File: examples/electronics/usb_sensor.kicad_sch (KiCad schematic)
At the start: 17 parts, among them J1 USB-Micro-B, J2 SWD, SW1 SPST, U1 AP2112K-3.3, U2 STM32F042, U3 SHT40

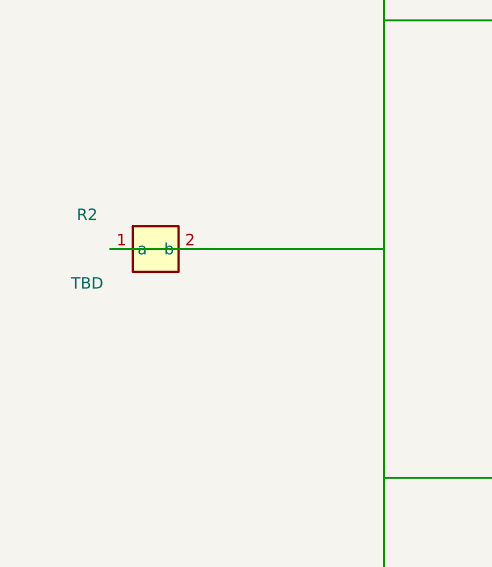
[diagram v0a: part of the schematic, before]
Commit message: feat(electronics): component laws Slice 5 — stdlib laws and fixtures
Add generic dimensioned law parameters on pin-bearing component types
(spec ForwardVoltage: Volt; spec DynamicResistance: Ohm;), including
type-level quantity defaults. Unknown spec names remain rejected outside
component bodies.

- stdlib Resistor and Wire declare always-active laws
- stdlib Diode and Led declare forward/reverse piecewise laws
- later component declarations shadow prelude declarations, so local
  same-named types cannot inherit stdlib laws by accident
- migrate led_blinker to stdlib laws and structured datasheet physics;
  the solver proves its 4.4 mA operating point
- migrate usb_sensor resistance values to structured specs; keep its
  local Resistor law-free until SPST conditional-topology state exists
- document the law mechanism and remaining fixture migration boundary

Full lib suite green; Praetor no new diagnostics; both fixtures emit.
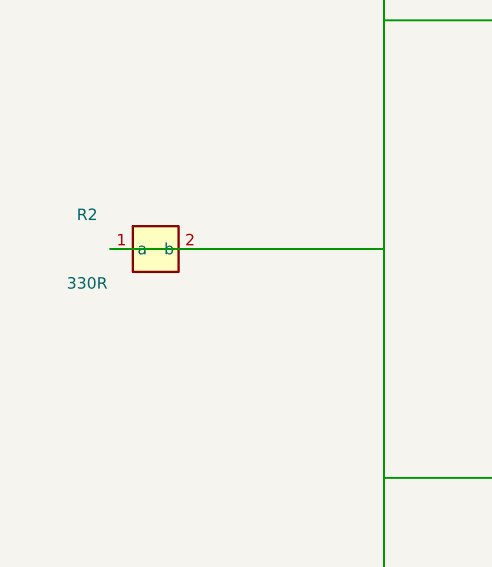
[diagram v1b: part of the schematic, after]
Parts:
- R2: value TBD -> 330R
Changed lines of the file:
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@@
     (in_bom yes) (on_board yes)
     (property "Reference" "R2" (at 93.98 300.99 0) (effects (font (size 1.27 1.27))))
-    (property "Value" "TBD" (at 93.98 308.61 0) (effects (font (size 1.27 1.27))))
+    (property "Value" "330R" (at 93.98 308.61 0) (effects (font (size 1.27 1.27))))
     (property "Footprint" "0603" (at 101.60 304.80 0) (effects (font (size 1.27 1.27)) (hide yes)))
     (instances (project briev

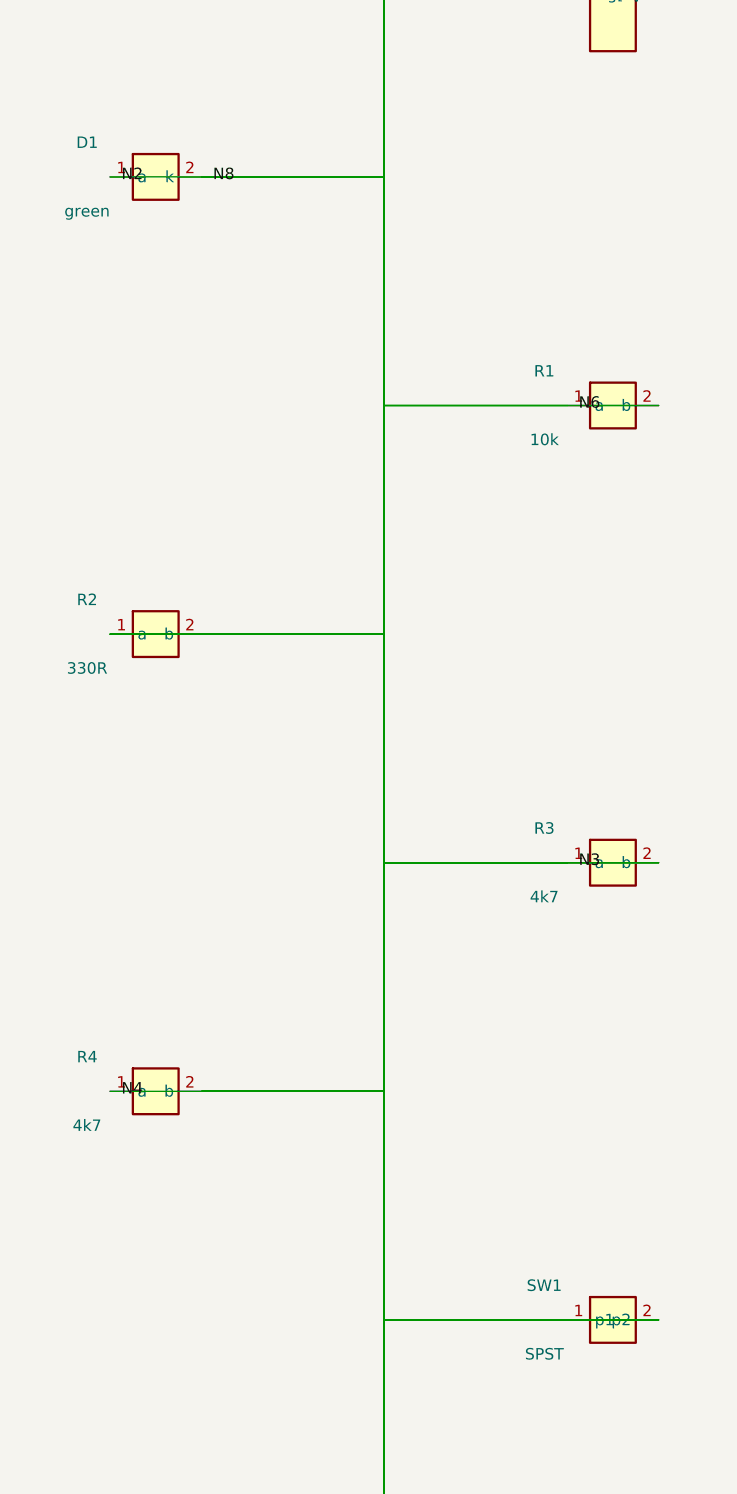
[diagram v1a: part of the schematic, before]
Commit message: feat(electronics): SPST component modes and node state selection
Add explicitly named finite component modes to the law substrate:

- parse contextual `mode <name> { … }` declarations in component bodies
- elaborate mode facts through the shared linear-law machinery
- enumerate every declared mode as a first-class DC operating state
- record instance→mode assignments and deterministic state labels
- select node-applicable states with `sw1.closed` / `!sw1.closed`
- prove node postconditions only in matching states while tolerance,
  rating, and budget checks remain all-state
- reject unknown modes and mode preconditions matching zero states
- add generic stdlib Spst with closed/open modes
- migrate usb_sensor to Spst, split pressed/released nodes, wire the
  button pull-up path, and make its local resistor law-bearing

Checked-in .ebv fixtures cover pressed/released selection and a typoed
mode selector. Full lib suite green; electronics fixtures emit; no new
Praetor diagnostics in touched analysis/parser/backend surfaces.
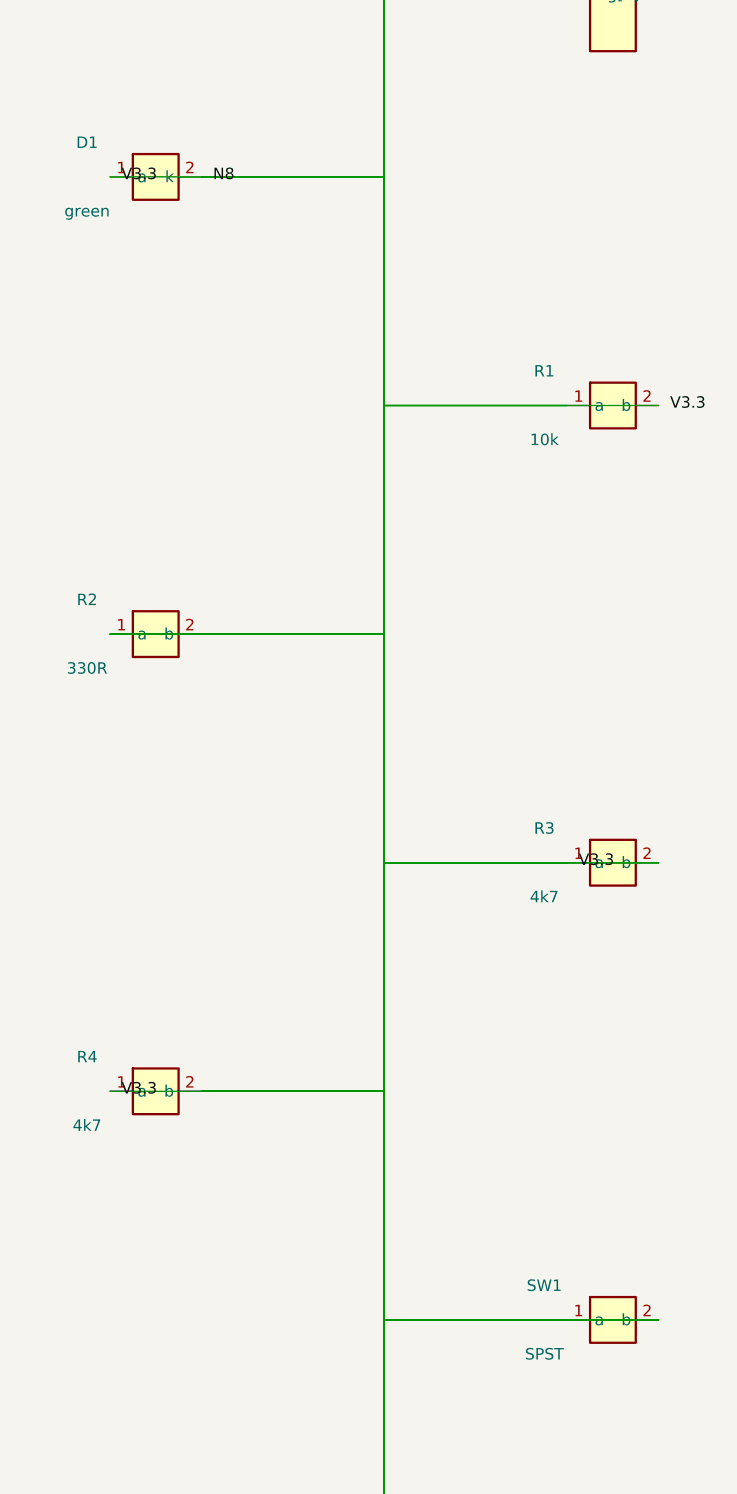
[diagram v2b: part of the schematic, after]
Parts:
- SW1: symbol Switch -> Spst
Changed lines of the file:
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@@
     ))
   )
-  (symbol (lib_id "Switch") (at 152.40 381.00 0) (unit 1)
+  (symbol (lib_id "Spst") (at 152.40 381.00 0) (unit 1)
     (in_bom yes) (on_board yes)
     (property "Reference" "SW1" (at 144.78 377.19 0) (effects (font (size 1.27 1.27))))
@@
   (wire (pts (xy 127.00 254.00) (xy 127.00 304.80)) (stroke (width 0) (type default)))
   (wire (pts (xy 127.00 304.80) (xy 106.68 304.80)) (stroke (width 0) (type default)))
-  (label "N2" (at 97.79 254.00 0) (effects (font (size 1.27 1.27)) (justify (left bottom))))
+  (label "V3.3" (at 97.79 254.00 0) (effects (font (size 1.27 1.27)) (justify (left bottom))))
   (wire (pts (xy 147.32 330.20) (xy 127.00 330.20)) (stroke (width 0) (type default)))
   (wire (pts (xy 127.00 330.20) (xy 127.00 431.80)) (stroke (width 0) (type default)))
@@
   (wire (pts (xy 127.00 431.80) (xy 127.00 455.93)) (stroke (width 0) (type default)))
   (wire (pts (xy 127.00 455.93) (xy 106.68 455.93)) (stroke (width 0) (type default)))
-  (label "N3" (at 148.59 330.20 0) (effects (font (size 1.27 1.27)) (justify (left bottom))))
+  (label "V3.3" (at 148.59 330.20 0) (effects (font (size 1.27 1.27)) (justify (left bottom))))
   (wire (pts (xy 96.52 355.60) (xy 127.00 355.60)) (stroke (width 0) (type default)))
   (wire (pts (xy 127.00 355.60) (xy 127.00 429.26)) (stroke (width 0) (type default)))
@@
   (wire (pts (xy 127.00 429.26) (xy 127.00 459.74)) (stroke (width 0) (type default)))
   (wire (pts (xy 127.00 459.74) (xy 96.52 459.74)) (stroke (width 0) (type default)))
-  (label "N4" (at 97.79 355.60 0) (effects (font (size 1.27 1.27)) (justify (left bottom))))
+  (label "V3.3" (at 97.79 355.60 0) (effects (font (size 1.27 1.27)) (justify (left bottom))))
   (wire (pts (xy 147.32 76.20) (xy 127.00 76.20)) (stroke (width 0) (type default)))
   (wire (pts (xy 127.00 76.20) (xy 127.00 101.60)) (stroke (width 0) (type default)))
@@
   (wire (pts (xy 157.48 232.41) (xy 127.00 232.41)) (stroke (width 0) (type default)))
   (wire (pts (xy 127.00 232.41) (xy 127.00 279.40)) (stroke (width 0) (type default)))
-  (wire (pts (xy 127.00 279.40) (xy 157.48 279.40)) (stroke (width 0) (type default)))
-  (wire (pts (xy 157.48 279.40) (xy 127.00 279.40)) (stroke (width 0) (type default)))
+  (wire (pts (xy 127.00 279.40) (xy 147.32 279.40)) (stroke (width 0) (type default)))
+  (wire (pts (xy 147.32 279.40) (xy 127.00 279.40)) (stroke (width 0) (type default)))
   (wire (pts (xy 127.00 279.40) (xy 127.00 304.80)) (stroke (width 0) (type default)))
   (wire (pts (xy 127.00 304.80) (xy 96.52 304.80)) (stroke (width 0) (type default)))
@@
   (wire (pts (xy 127.00 454.66) (xy 96.52 454.66)) (stroke (width 0) (type default)))
   (label "V3.3" (at 148.59 76.20 0) (effects (font (size 1.27 1.27)) (justify (left bottom))))
-  (wire (pts (xy 147.32 279.40) (xy 127.00 279.40)) (stroke (width 0) (type default)))
+  (wire (pts (xy 157.48 279.40) (xy 127.00 279.40)) (stroke (width 0) (type default)))
   (wire (pts (xy 127.00 279.40) (xy 127.00 381.00)) (stroke (width 0) (type default)))
   (wire (pts (xy 127.00 381.00) (xy 147.32 381.00)) (stroke (width 0) (type default)))
@@
   (wire (pts (xy 127.00 381.00) (xy 127.00 435.61)) (stroke (width 0) (type default)))
   (wire (pts (xy 127.00 435.61) (xy 147.32 435.61)) (stroke (width 0) (type default)))
-  (label "N6" (at 148.59 279.40 0) (effects (font (size 1.27 1.27)) (justify (left bottom))))
+  (label "V3.3" (at 158.75 279.40 0) (effects (font (size 1.27 1.27)) (justify (left bottom))))
   (wire (pts (xy 96.52 50.80) (xy 127.00 50.80)) (stroke (width 0) (type default)))
   (wire (pts (xy 127.00 50.80) (xy 127.00 177.80)) (stroke (width 0) (type default)))
